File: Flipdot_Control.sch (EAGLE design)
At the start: 7 parts

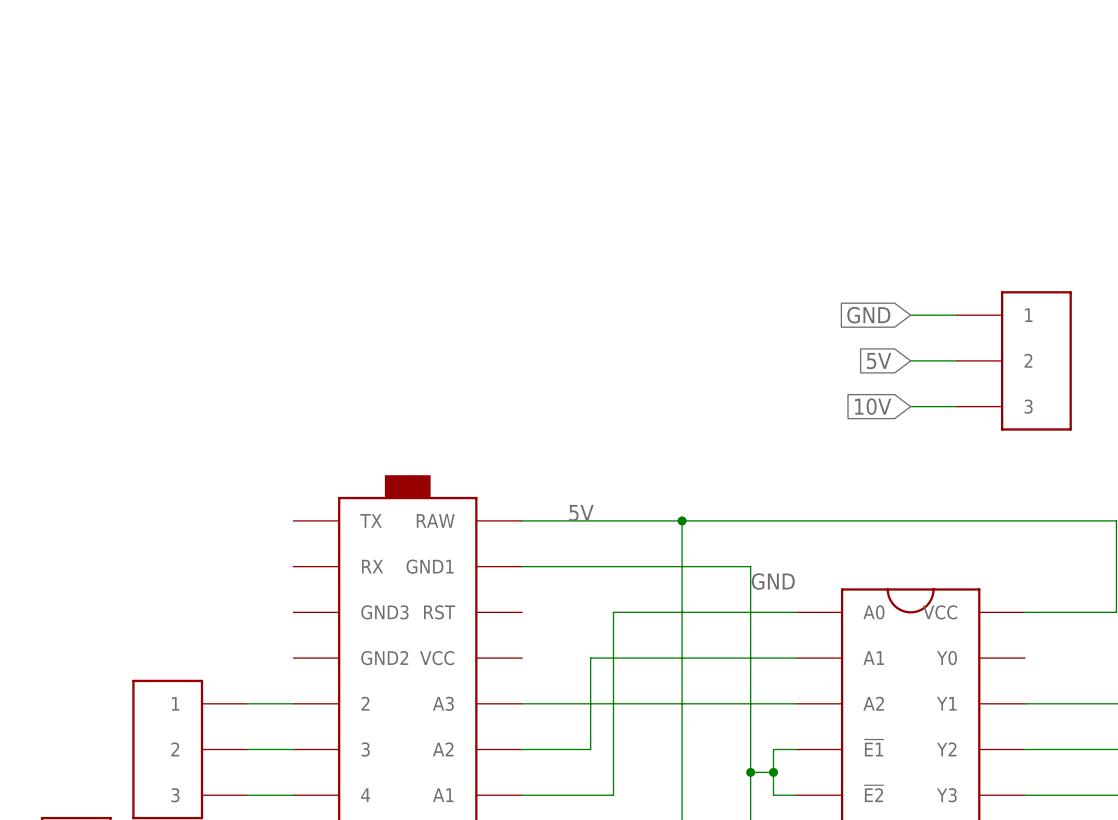
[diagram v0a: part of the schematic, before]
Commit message: Added power regulators to control board
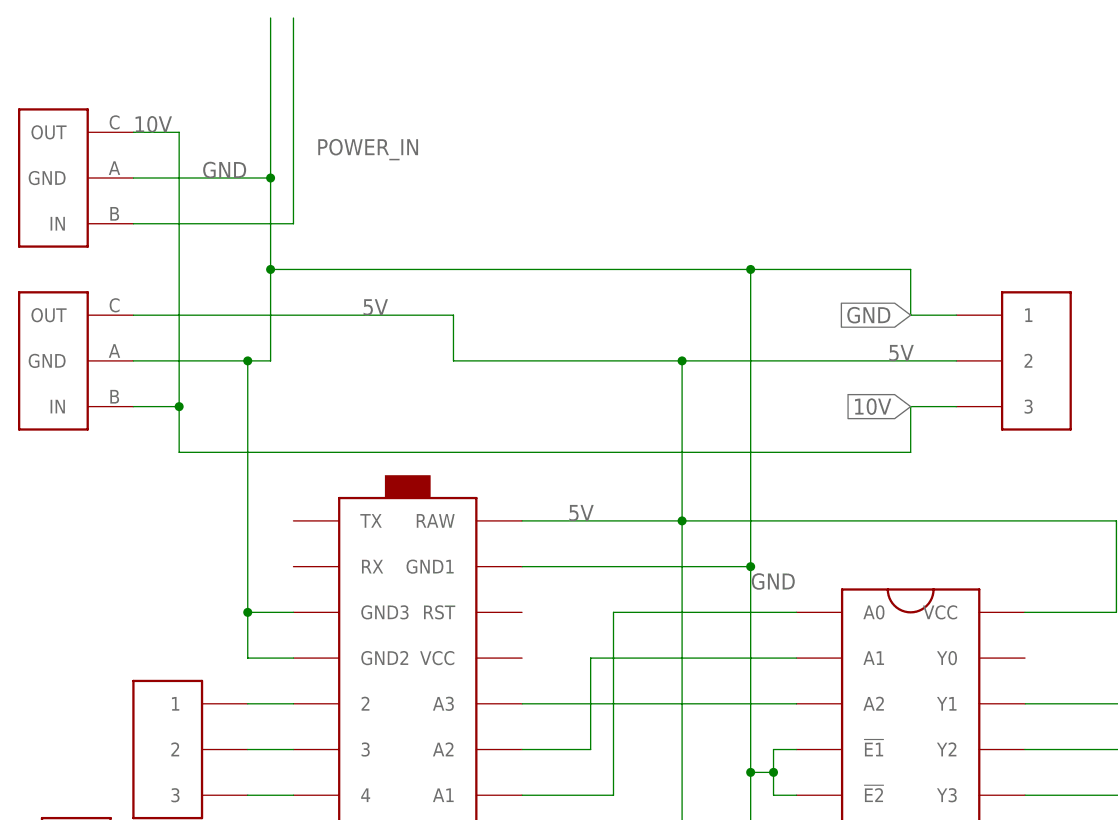
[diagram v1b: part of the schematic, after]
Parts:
- added U$8, U$9: POWER, Flipdot:POWER
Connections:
- new net POWER_IN: U$9.IN
- net 10V: now also U$8.IN, U$9.OUT
- net 5V: now also U$8.OUT
- net GND: now also U$1.GND2, U$1.GND3, U$8.GND, U$9.GND
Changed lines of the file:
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@@
 <part name="U$6" library="Flipdot" deviceset="3_PIN" device=""/>
 <part name="U$7" library="Flipdot" deviceset="3_PIN" device=""/>
+<part name="U$8" library="Flipdot" deviceset="POWER" device=""/>
+<part name="U$9" library="Flipdot" deviceset="POWER" device=""/>
 </parts>
 <sheets>
@@
 <instance part="U$6" gate="G$1" x="-68.58" y="-7.62" rot="MR0"/>
 <instance part="U$7" gate="G$1" x="30.48" y="50.8"/>
+<instance part="U$8" gate="G$1" x="-71.12" y="50.8" rot="R180"/>
+<instance part="U$9" gate="G$1" x="-71.12" y="71.12" rot="R180"/>
 </instances>
 <busses>
@@
 <junction x="-5.08" y="33.02"/>
 <label x="-17.78" y="33.02" size="1.778" layer="95"/>
-</segment>
-<segment>
+<pinref part="U$8" gate="G$1" pin="OUT"/>
+<wire x1="-66.04" y1="55.88" x2="-30.48" y2="55.88" width="0.1524" layer="91"/>
+<label x="-40.64" y="55.88" size="1.778" layer="95"/>
 <pinref part="U$7" gate="G$1" pin="2"/>
-<wire x1="25.4" y1="50.8" x2="20.32" y2="50.8" width="0.1524" layer="91"/>
-<label x="20.32" y="50.8" size="1.778" layer="95" rot="R180" xref="yes"/>
+<wire x1="-30.48" y1="55.88" x2="-30.48" y2="50.8" width="0.1524" layer="91"/>
+<wire x1="-30.48" y1="50.8" x2="-5.08" y2="50.8" width="0.1524" layer="91"/>
+<label x="17.78" y="50.8" size="1.778" layer="95"/>
+<wire x1="-5.08" y1="50.8" x2="25.4" y2="50.8" width="0.1524" layer="91"/>
+<wire x1="-5.08" y1="33.02" x2="-5.08" y2="50.8" width="0.1524" layer="91"/>
+<junction x="-5.08" y="50.8"/>
 </segment>
 </net>
@@
 <wire x1="2.54" y1="27.94" x2="-22.86" y2="27.94" width="0.1524" layer="91"/>
 <label x="2.54" y="25.4" size="1.778" layer="95"/>
-</segment>
-<segment>
 <pinref part="U$7" gate="G$1" pin="1"/>
 <wire x1="25.4" y1="55.88" x2="20.32" y2="55.88" width="0.1524" layer="91"/>
 <label x="20.32" y="55.88" size="1.778" layer="95" rot="R180" xref="yes"/>
+<pinref part="U$9" gate="G$1" pin="GND"/>
+<wire x1="-66.04" y1="71.12" x2="-50.8" y2="71.12" width="0.1524" layer="91"/>
+<wire x1="-50.8" y1="71.12" x2="-50.8" y2="88.9" width="0.1524" layer="91"/>
+<label x="-58.42" y="71.12" size="1.778" layer="95"/>
+<pinref part="U$8" gate="G$1" pin="GND"/>
+<wire x1="-66.04" y1="50.8" x2="-53.34" y2="50.8" width="0.1524" layer="91"/>
+<wire x1="-53.34" y1="50.8" x2="-50.8" y2="50.8" width="0.1524" layer="91"/>
+<wire x1="-50.8" y1="50.8" x2="-50.8" y2="60.96" width="0.1524" layer="91"/>
+<junction x="-50.8" y="71.12"/>
+<wire x1="-50.8" y1="60.96" x2="-50.8" y2="71.12" width="0.1524" layer="91"/>
+<wire x1="20.32" y1="55.88" x2="20.32" y2="60.96" width="0.1524" layer="91"/>
+<wire x1="20.32" y1="60.96" x2="2.54" y2="60.96" width="0.1524" layer="91"/>
+<junction x="-50.8" y="60.96"/>
+<wire x1="2.54" y1="60.96" x2="-50.8" y2="60.96" width="0.1524" layer="91"/>
+<wire x1="2.54" y1="27.94" x2="2.54" y2="60.96" width="0.1524" layer="91"/>
+<junction x="2.54" y="27.94"/>
+<junction x="2.54" y="60.96"/>
+<pinref part="U$1" gate="G$1" pin="GND2"/>
+<wire x1="-48.26" y1="17.78" x2="-53.34" y2="17.78" width="0.1524" layer="91"/>
+<wire x1="-53.34" y1="17.78" x2="-53.34" y2="22.86" width="0.1524" layer="91"/>
+<pinref part="U$1" gate="G$1" pin="GND3"/>
+<wire x1="-53.34" y1="22.86" x2="-48.26" y2="22.86" width="0.1524" layer="91"/>
+<wire x1="-53.34" y1="22.86" x2="-53.34" y2="50.8" width="0.1524" layer="91"/>
+<junction x="-53.34" y="22.86"/>
+<junction x="-53.34" y="50.8"/>
 </segment>
 </net>
@@
 <wire x1="25.4" y1="45.72" x2="20.32" y2="45.72" width="0.1524" layer="91"/>
 <label x="20.32" y="45.72" size="1.778" layer="95" rot="R180" xref="yes"/>
-</segment>
-</net>
+<wire x1="20.32" y1="45.72" x2="20.32" y2="40.64" width="0.1524" layer="91"/>
+<pinref part="U$9" gate="G$1" pin="OUT"/>
+<wire x1="-66.04" y1="76.2" x2="-60.96" y2="76.2" width="0.1524" layer="91"/>
+<wire x1="-60.96" y1="76.2" x2="-60.96" y2="45.72" width="0.1524" layer="91"/>
+<pinref part="U$8" gate="G$1" pin="IN"/>
+<wire x1="-60.96" y1="45.72" x2="-66.04" y2="45.72" width="0.1524" layer="91"/>
+<label x="-66.04" y="76.2" size="1.778" layer="95"/>
+<wire x1="20.32" y1="40.64" x2="-60.96" y2="40.64" width="0.1524" layer="91"/>
+<wire x1="-60.96" y1="40.64" x2="-60.96" y2="45.72" width="0.1524" layer="91"/>
+<junction x="-60.96" y="45.72"/>
+</segment>
+</net>
+<net name="POWER_IN" class="0">
+<segment>
+<pinref part="U$9" gate="G$1" pin="IN"/>
+<wire x1="-66.04" y1="66.04" x2="-48.26" y2="66.04" width="0.1524" layer="91"/>
+<wire x1="-48.26" y1="66.04" x2="-48.26" y2="88.9" width="0.1524" layer="91"/>
+<label x="-45.72" y="73.66" size="1.778" layer="95"/>
+</segment>
+</net>

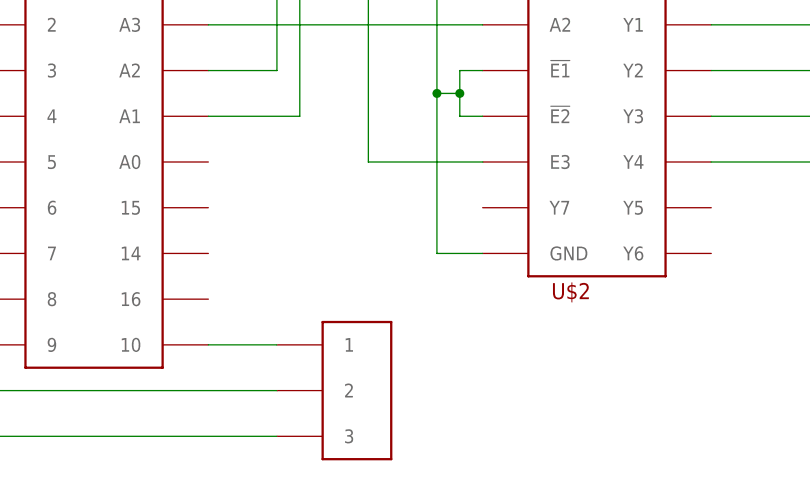
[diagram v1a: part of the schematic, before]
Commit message: Fixed missing RE connector
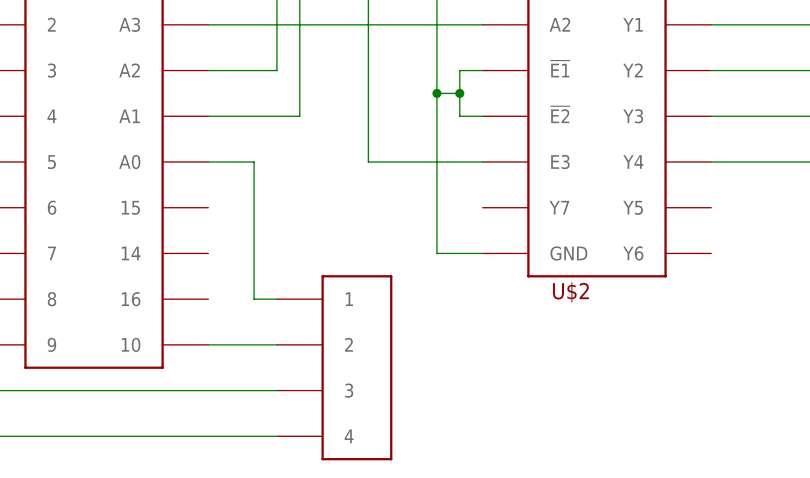
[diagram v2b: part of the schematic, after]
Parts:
- U$4: value 3_PIN -> 4_PIN; device Flipdot:3_PIN -> Flipdot:4_PIN
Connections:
- new net N$17: U$1.A0, U$4.1
- net N$10: now also U$4.4; no longer U$4.3
- net N$8: now also U$4.2; no longer U$4.1
- net N$9: now also U$4.3; no longer U$4.2
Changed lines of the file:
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@@
 <?xml version="1.0" encoding="utf-8"?>
 <!DOCTYPE eagle SYSTEM "eagle.dtd">
-<eagle version="9.1.3">
+<eagle version="9.2.2">
 <drawing>
 <settings>
@@
 <part name="U$2" library="Flipdot" deviceset="74HC238" device="" package3d_urn="urn:adsk.eagle:package:28986/2"/>
 <part name="U$3" library="Flipdot" deviceset="4_PIN" device=""/>
-<part name="U$4" library="Flipdot" deviceset="3_PIN" device=""/>
 <part name="U$5" library="Flipdot" deviceset="3_PIN" device=""/>
 <part name="U$6" library="Flipdot" deviceset="3_PIN" device=""/>
@@
 <part name="U$8" library="Flipdot" deviceset="POWER" device=""/>
 <part name="U$9" library="Flipdot" deviceset="POWER" device=""/>
+<part name="U$4" library="Flipdot" deviceset="4_PIN" device=""/>
 </parts>
 <sheets>
@@
 </plain>
 <instances>
-<instance part="U$1" gate="G$1" x="-35.56" y="5.08" rot="R270"/>
-<instance part="U$2" gate="G$1" x="20.32" y="5.08" rot="R270"/>
-<instance part="U$3" gate="G$1" x="50.8" y="5.08"/>
-<instance part="U$4" gate="G$1" x="-10.16" y="-27.94"/>
-<instance part="U$5" gate="G$1" x="-58.42" y="7.62" rot="MR0"/>
-<instance part="U$6" gate="G$1" x="-68.58" y="-7.62" rot="MR0"/>
-<instance part="U$7" gate="G$1" x="30.48" y="50.8"/>
-<instance part="U$8" gate="G$1" x="-71.12" y="50.8" rot="R180"/>
-<instance part="U$9" gate="G$1" x="-71.12" y="71.12" rot="R180"/>
+<instance part="U$1" gate="G$1" x="-35.56" y="5.08" smashed="yes" rot="R270"/>
+<instance part="U$2" gate="G$1" x="20.32" y="5.08" smashed="yes" rot="R270">
+<attribute name="NAME" x="15.24" y="-17.78" size="1.778" layer="94"/>
+</instance>
+<instance part="U$3" gate="G$1" x="50.8" y="5.08" smashed="yes"/>
+<instance part="U$5" gate="G$1" x="-58.42" y="7.62" smashed="yes" rot="MR0"/>
+<instance part="U$6" gate="G$1" x="-68.58" y="-7.62" smashed="yes" rot="MR0"/>
+<instance part="U$7" gate="G$1" x="30.48" y="50.8" smashed="yes"/>
+<instance part="U$8" gate="G$1" x="-71.12" y="50.8" smashed="yes" rot="R180"/>
+<instance part="U$9" gate="G$1" x="-71.12" y="71.12" smashed="yes" rot="R180"/>
+<instance part="U$4" gate="G$1" x="-10.16" y="-25.4" smashed="yes"/>
 </instances>
 <busses>
@@
 <segment>
 <pinref part="U$1" gate="G$1" pin="10"/>
-<pinref part="U$4" gate="G$1" pin="1"/>
 <wire x1="-22.86" y1="-22.86" x2="-15.24" y2="-22.86" width="0.1524" layer="91"/>
+<pinref part="U$4" gate="G$1" pin="2"/>
 </segment>
 </net>
@@
 <wire x1="-48.26" y1="-22.86" x2="-53.34" y2="-22.86" width="0.1524" layer="91"/>
 <wire x1="-53.34" y1="-22.86" x2="-53.34" y2="-27.94" width="0.1524" layer="91"/>
-<pinref part="U$4" gate="G$1" pin="2"/>
 <wire x1="-53.34" y1="-27.94" x2="-15.24" y2="-27.94" width="0.1524" layer="91"/>
+<pinref part="U$4" gate="G$1" pin="3"/>
 </segment>
 </net>
@@
 <wire x1="-48.26" y1="-17.78" x2="-58.42" y2="-17.78" width="0.1524" layer="91"/>
 <wire x1="-58.42" y1="-17.78" x2="-58.42" y2="-33.02" width="0.1524" layer="91"/>
-<pinref part="U$4" gate="G$1" pin="3"/>
 <wire x1="-58.42" y1="-33.02" x2="-15.24" y2="-33.02" width="0.1524" layer="91"/>
+<pinref part="U$4" gate="G$1" pin="4"/>
 </segment>
 </net>
@@
 </segment>
 </net>
+<net name="N$17" class="0">
+<segment>
+<pinref part="U$1" gate="G$1" pin="A0"/>
+<wire x1="-22.86" y1="-2.54" x2="-17.78" y2="-2.54" width="0.1524" layer="91"/>
+<wire x1="-17.78" y1="-2.54" x2="-17.78" y2="-17.78" width="0.1524" layer="91"/>
+<pinref part="U$4" gate="G$1" pin="1"/>
+<wire x1="-17.78" y1="-17.78" x2="-15.24" y2="-17.78" width="0.1524" layer="91"/>
+</segment>
+</net>

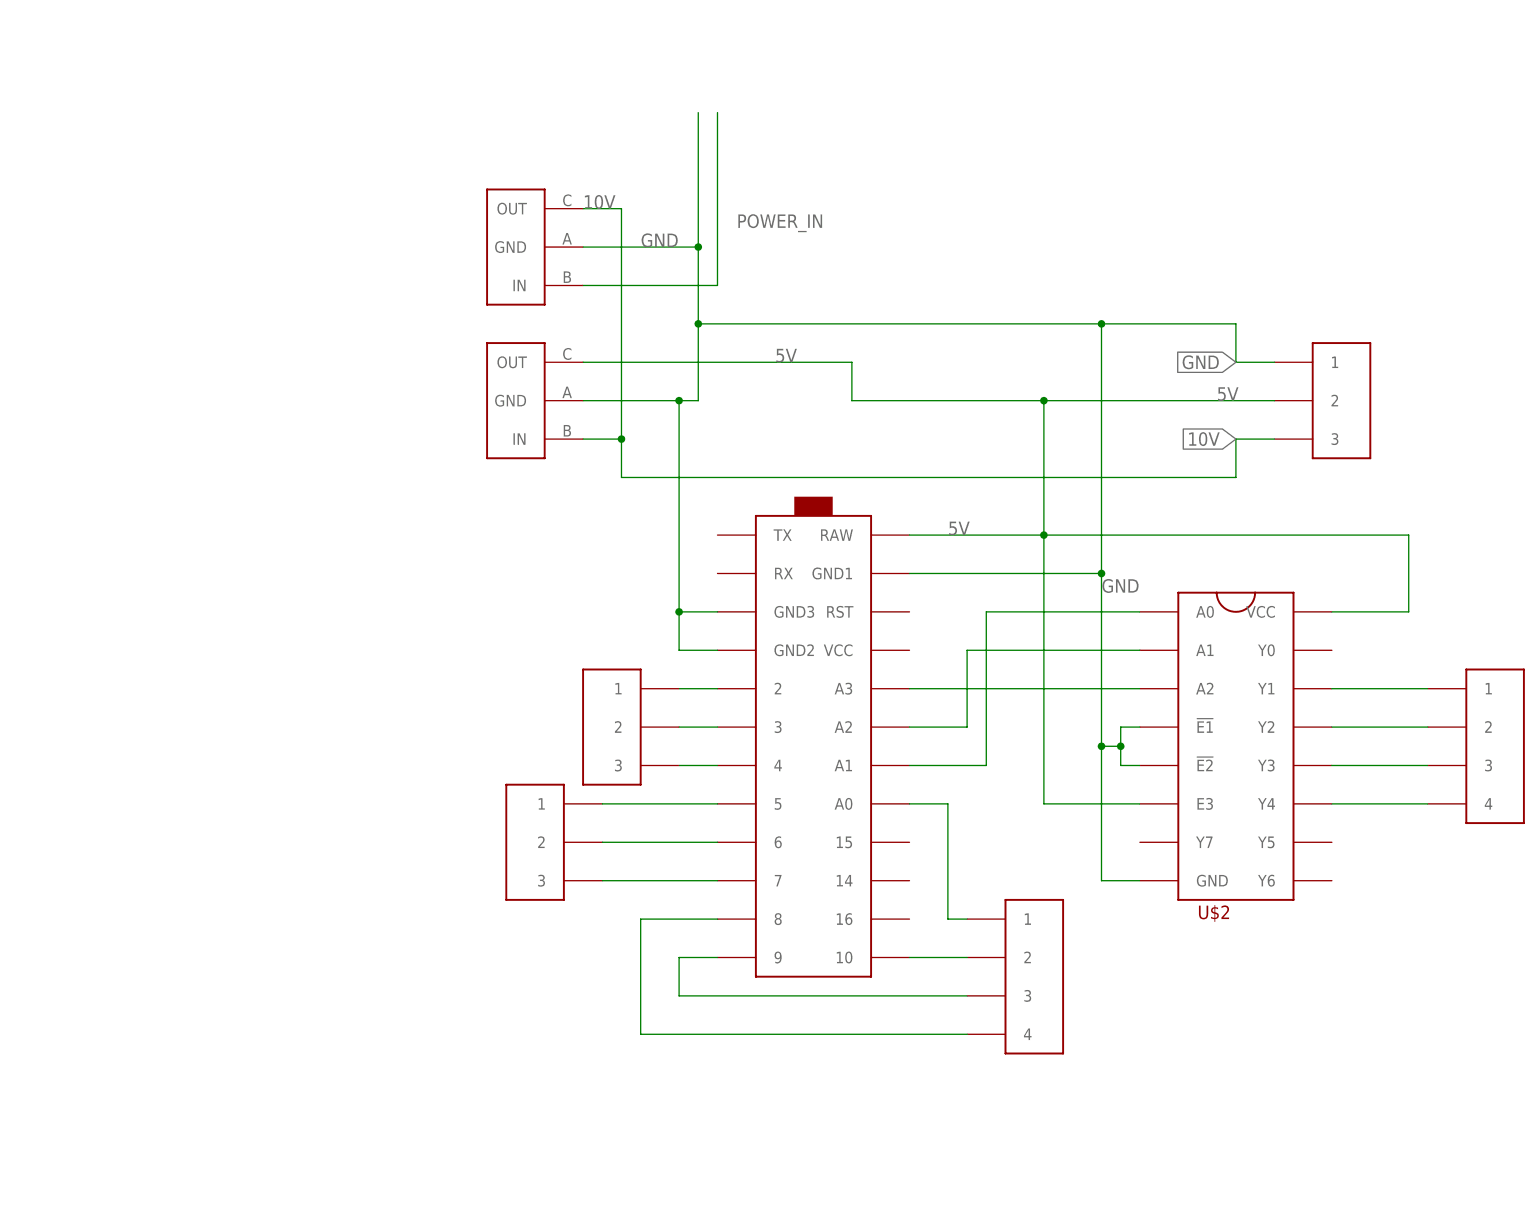
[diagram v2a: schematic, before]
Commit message: Remapped outputs, replaced MCU
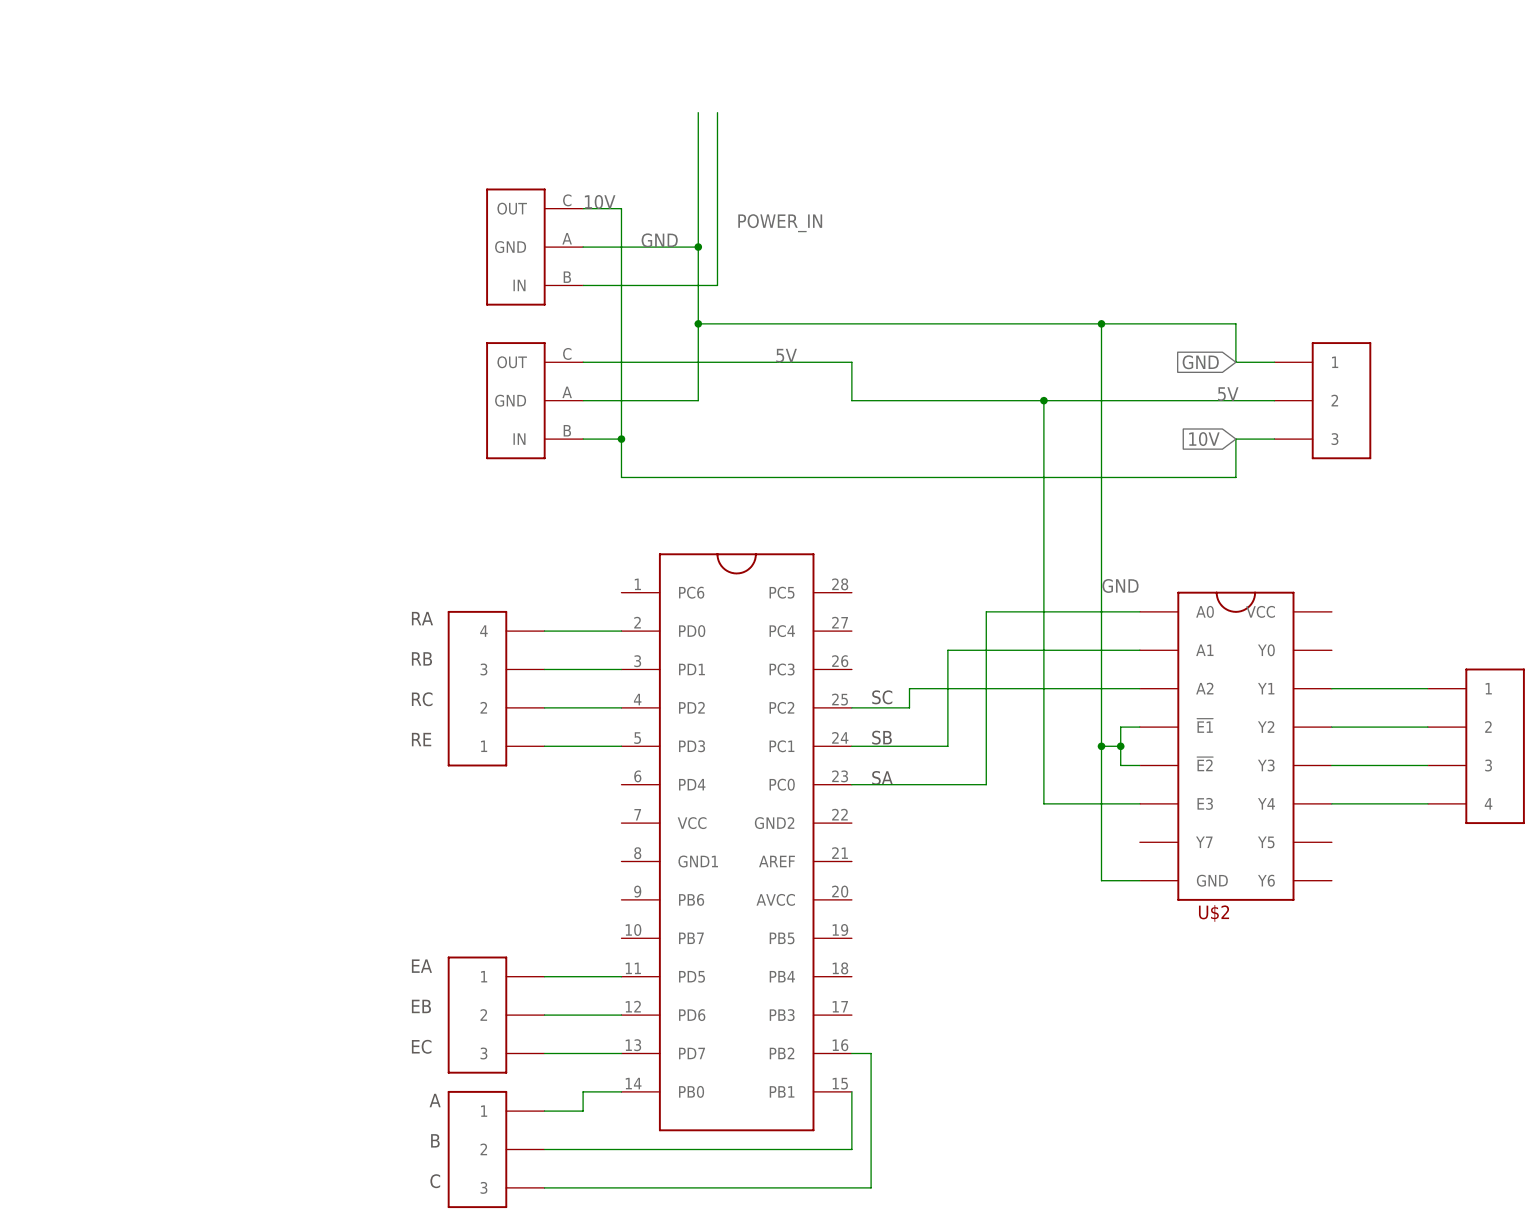
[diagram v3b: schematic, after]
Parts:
- removed U$1: MCU, Flipdot:MCU
- added U$10: ATMEGA328P, Flipdot:ATMEGA328P
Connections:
- removed net N$17: U$1.A0, U$4.1
- new net N$18: U$10.PD5, U$6.1
- net 5V: no longer U$1.RAW, U$2.VCC
- net GND: no longer U$1.GND1, U$1.GND2, U$1.GND3
- net N$10: now also U$10.PD2, U$4.2; no longer U$1.8, U$4.4
- net N$11: now also U$10.PB0; no longer U$1.2
- net N$12: now also U$10.PB1; no longer U$1.3
- net N$13: now also U$10.PB2; no longer U$1.4
- net N$14: now also U$10.PD3, U$4.1; no longer U$1.5, U$6.1
- net N$15: now also U$10.PD7, U$6.3; no longer U$1.6, U$6.2
- net N$16: now also U$10.PD6, U$6.2; no longer U$1.7, U$6.3
- net N$5: now also U$10.PC0; no longer U$1.A1
- net N$6: now also U$10.PC1; no longer U$1.A2
- net N$7: now also U$10.PC2; no longer U$1.A3
- net N$8: now also U$10.PD0, U$4.4; no longer U$1.10, U$4.2
- net N$9: now also U$10.PD1; no longer U$1.9
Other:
- note added: "A B C"
- note added: "EA EB EC"
- note added: "RA RB RC RE"
- note added: "SC SB SA"
